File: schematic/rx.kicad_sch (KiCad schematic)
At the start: 32 parts, among them Q12 2N3904, U11 ADE-1L

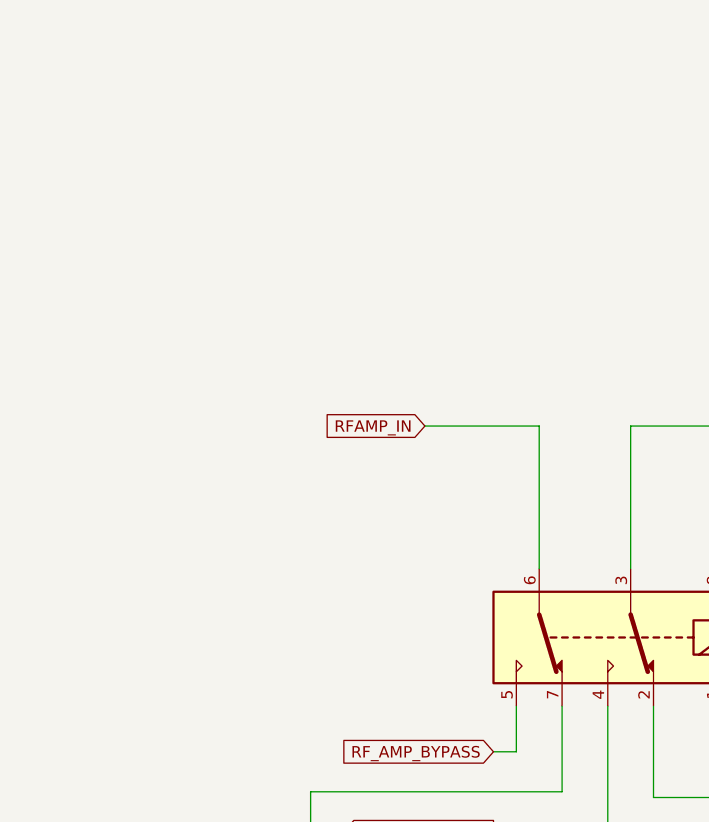
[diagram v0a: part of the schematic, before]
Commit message: Add /TX Common/ schematic sheet
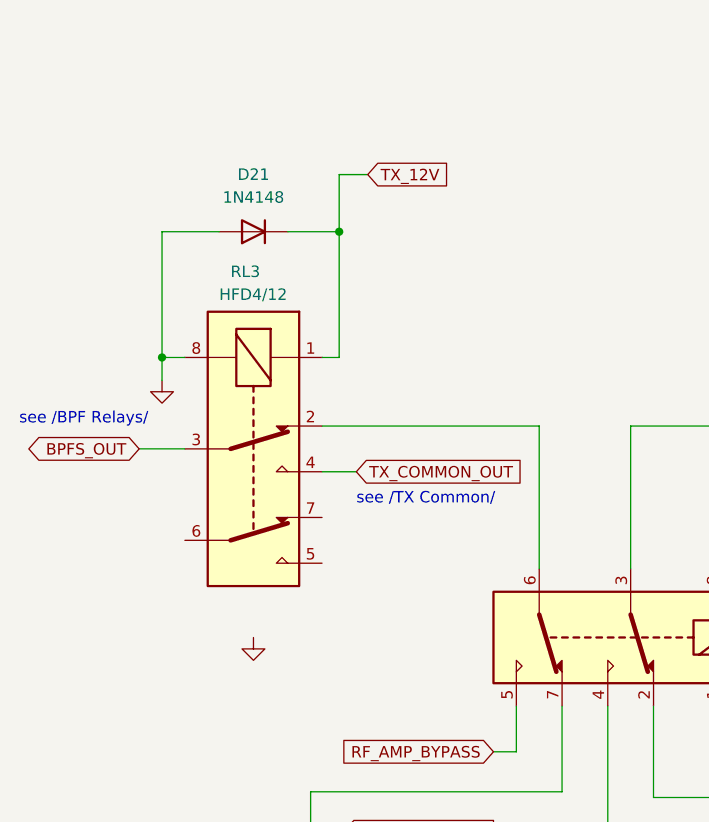
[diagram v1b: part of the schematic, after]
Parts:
- added D21: 1N4148, Diode_THT:D_DO-35_SOD27_P7.62mm_Horizontal, symbol Diode:1N4148
- added RL3: HFD4/12, Relay_THT:Relay_DPDT_Omron_G2RL, symbol Relay:G2RL-2-ASI-DC5
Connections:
- net GND: now also D21.2 (A), RL3.8
- net RFAMP_IN: no longer names the net of RL3.6
- net RFAMP_IN: now also RL3.2
- new net BPFS_OUT: RL3.3
- new net TX_12V: D21.1 (K), RL3.1
- new net TX_COMMON_OUT: RL3.4
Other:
- note added: "see /BPF Relays/"
- note added: "see /TX Common/"
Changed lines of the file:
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@@
   (junction (at 175.895 71.755) (diameter 0) (color 0 0 0 0)
   )
+  (junction (at 52.705 43.18) (diameter 0) (color 0 0 0 0)
+  )
+  (junction (at 33.02 57.15) (diameter 0) (color 0 0 0 0)
+  )
   (junction (at 196.215 45.085) (diameter 0) (color 0 0 0 0)
   )
@@
     (stroke (width 0) (type default))
   )
+  (wire (pts (xy 33.02 57.15) (xy 35.56 57.15))
+    (stroke (width 0) (type default))
+  )
   (wire (pts (xy 85.725 128.27) (xy 85.725 142.24))
     (stroke (width 0) (type default))
   )
+  (wire (pts (xy 33.02 43.18) (xy 39.37 43.18))
+    (stroke (width 0) (type default))
+  )
   (wire (pts (xy 220.98 75.565) (xy 220.98 78.105))
     (stroke (width 0) (type default))
@@
     (stroke (width 0) (type default))
   )
-  (wire (pts (xy 62.23 64.77) (xy 74.93 64.77))
+  (wire (pts (xy 50.8 64.77) (xy 74.93 64.77))
     (stroke (width 0) (type default))
   )
@@
     (stroke (width 0) (type default))
   )
+  (wire (pts (xy 33.02 57.15) (xy 33.02 43.18))
+    (stroke (width 0) (type default))
+  )
   (wire (pts (xy 174.625 52.07) (xy 175.895 52.07))
     (stroke (width 0) (type default))
@@
     (stroke (width 0) (type default))
   )
+  (wire (pts (xy 46.99 43.18) (xy 52.705 43.18))
+    (stroke (width 0) (type default))
+  )
+  (wire (pts (xy 52.705 36.83) (xy 52.705 43.18))
+    (stroke (width 0) (type default))
+  )
   (wire (pts (xy 189.23 31.115) (xy 200.025 31.115))
     (stroke (width 0) (type default))
@@
     (stroke (width 0) (type default))
   )
+  (wire (pts (xy 33.02 59.69) (xy 33.02 57.15))
+    (stroke (width 0) (type default))
+  )
   (wire (pts (xy 112.395 161.925) (xy 116.205 161.925))
     (stroke (width 0) (type default))
@@
     (stroke (width 0) (type default))
   )
+  (wire (pts (xy 52.705 43.18) (xy 52.705 57.15))
+    (stroke (width 0) (type default))
+  )
   (wire (pts (xy 95.25 97.79) (xy 111.76 97.79))
     (stroke (width 0) (type default))
@@
     (stroke (width 0) (type default))
   )
+  (wire (pts (xy 50.8 69.85) (xy 54.61 69.85))
+    (stroke (width 0) (type default))
+  )
   (wire (pts (xy 179.07 31.115) (xy 184.15 31.115))
     (stroke (width 0) (type default))
@@
     (stroke (width 0) (type default))
   )
+  (wire (pts (xy 55.88 36.83) (xy 52.705 36.83))
+    (stroke (width 0) (type default))
+  )
   (wire (pts (xy 220.98 64.77) (xy 226.695 64.77))
     (stroke (width 0) (type default))
   )
+  (wire (pts (xy 52.705 57.15) (xy 50.8 57.15))
+    (stroke (width 0) (type default))
+  )
   (wire (pts (xy 82.55 179.07) (xy 82.55 181.61))
     (stroke (width 0) (type default))
@@
   )
   (wire (pts (xy 82.55 149.225) (xy 82.55 156.845))
+    (stroke (width 0) (type default))
+  )
+  (wire (pts (xy 30.48 67.31) (xy 35.56 67.31))
     (stroke (width 0) (type default))
   )
@@
     (effects (font (size 1.27 1.27)) (justify left bottom))
   )
+  (text "see /TX Common/" (at 54.61 73.66 0)
+    (effects (font (size 1.27 1.27)) (justify left bottom))
+  )
+  (text "see /BPF Relays/" (at 17.145 64.77 0)
+    (effects (font (size 1.27 1.27)) (justify left bottom))
+  )
   (text "10T bifilar\n@ T37-43" (at 88.9 149.225 0)
     (effects (font (size 1.27 1.27)) (justify left bottom))
@@
   (text "Buffer: amp + 6 dB attenuator" (at 168.91 104.14 0)
     (effects (font (size 1.27 1.27)) (justify left bottom))
+  )
+  (global_label "TX_12V" (shape input) (at 55.88 36.83 0) (fields_autoplaced)
+    (effects (font (size 1.27 1.27)) (justify left))
+    (property "Intersheetrefs" "${INTERSHEET_REFS}" (at 65.4381 36.83 0)
+      (effects (font (size 1.27 1.27)) (justify left) hide)
+    )
   )
   (global_label "XFLT_RX_IN" (shape output) (at 226.695 64.77 0) (fields_autoplaced)
@@
     )
   )
-  (global_label "RFAMP_IN" (shape input) (at 62.23 64.77 180) (fields_autoplaced)
-    (effects (font (size 1.27 1.27)) (justify right))
-    (property "Intersheetrefs" "${INTERSHEET_REFS}" (at 50.2527 64.77 0)
-      (effects (font (size 1.27 1.27)) (justify right) hide)
-    )
-  )
   (global_label "RF_AMP_BYPASS" (shape input) (at 69.85 100.965 180) (fields_autoplaced)
     (effects (font (size 1.27 1.27)) (justify right))
@@
     )
   )
+  (global_label "BPFS_OUT" (shape bidirectional) (at 30.48 67.31 180) (fields_autoplaced)
+    (effects (font (size 1.27 1.27)) (justify right))
+    (property "Intersheetrefs" "${INTERSHEET_REFS}" (at 17.0286 67.31 0)
+      (effects (font (size 1.27 1.27)) (justify right) hide)
+    )
+  )
   (global_label "RF_AMP_BYPASS" (shape output) (at 69.85 109.855 180) (fields_autoplaced)
     (effects (font (size 1.27 1.27)) (justify right))
@@
     )
   )
+  (global_label "TX_COMMON_OUT" (shape input) (at 54.61 69.85 0) (fields_autoplaced)
+    (effects (font (size 1.27 1.27)) (justify left))
+    (property "Intersheetrefs" "${INTERSHEET_REFS}" (at 73.421 69.85 0)
+      (effects (font (size 1.27 1.27)) (justify left) hide)
+    )
+  )
   (global_label "RX_12V" (shape input) (at 196.85 17.145 180) (fields_autoplaced)
     (effects (font (size 1.27 1.27)) (justify right))
@@
     )
   )
+  (symbol (lib_id "Diode:1N4148") (at 43.18 43.18 180) (unit 1)
+    (in_bom yes) (on_board yes) (dnp no) (fields_autoplaced)
+    (property "Reference" "D21" (at 43.18 36.83 0)
+      (effects (font (size 1.27 1.27)))
+    )
+    (property "Value" "1N4148" (at 43.18 39.37 0)
+      (effects (font (size 1.27 1.27)))
+    )
+    (property "Footprint" "Diode_THT:D_DO-35_SOD27_P7.62mm_Horizontal" (at 43.18 43.18 0)
+      (effects (font (size 1.27 1.27)) hide)
+    )
+    (property "Datasheet" "https://assets.nexperia.com/documents/data-sheet/1N4148_1N4448.pdf" (at 43.18 43.18 0)
+      (effects (font (size 1.27 1.27)) hide)
+    )
+    (property "Sim.Device" "D" (at 43.18 43.18 0)
+      (effects (font (size 1.27 1.27)) hide)
+    )
+    (property "Sim.Pins" "1=K 2=A" (at 43.18 43.18 0)
+      (effects (font (size 1.27 1.27)) hide)
+    )
+    (pin "1")
+    (pin "2")
+    (instances
+      (project "hbr-mk2"
+        (path "/700c9878-4ed7-49d5-a273-77cf9d92989d/510b993f-d652-41da-8b0c-b7668be8d7c3"
+          (reference "D21") (unit 1)
+        )
+      )
+    )
+  )
   (symbol (lib_id "power:GND") (at 200.025 43.815 0) (unit 1)
     (in_bom yes) (on_board yes) (dnp no) (fields_autoplaced)
@@
     )
   )
+  (symbol (lib_id "power:GND") (at 33.02 59.69 0) (unit 1)
+    (in_bom yes) (on_board yes) (dnp no) (fields_autoplaced)
+    (property "Reference" "#PWR0130" (at 33.02 66.04 0)
+      (effects (font (size 1.27 1.27)) hide)
+    )
+    (property "Value" "GND" (at 33.02 64.77 0)
+      (effects (font (size 1.27 1.27)) hide)
+    )
+    (property "Footprint" "" (at 33.02 59.69 0)
+      (effects (font (size 1.27 1.27)) hide)
+    )
+    (property "Datasheet" "" (at 33.02 59.69 0)
+      (effects (font (size 1.27 1.27)) hide)
+    )
+    (pin "1")
+    (instances
+      (project "hbr-mk2"
+        (path "/700c9878-4ed7-49d5-a273-77cf9d92989d/0b45878c-17b8-4be8-9884-0f2bddd34788"
+          (reference "#PWR0130") (unit 1)
+        )
+        (path "/700c9878-4ed7-49d5-a273-77cf9d92989d/510b993f-d652-41da-8b0c-b7668be8d7c3"
+          (reference "#PWR0253") (unit 1)
+        )
+      )
+    )
+  )
   (symbol (lib_id "Device:R") (at 215.265 64.77 90) (unit 1)
     (in_bom yes) (on_board yes) (dnp no) (fields_autoplaced)
@@
     )
   )
+  (symbol (lib_id "Relay:G2RL-2-ASI-DC5") (at 43.18 67.31 270) (unit 1)
+    (in_bom yes) (on_board yes) (dnp no)
+    (property "Reference" "RL3" (at 40.64 47.625 90)
+      (effects (font (size 1.27 1.27)) (justify left))
+    )
+    (property "Value" "HFD4/12" (at 39.37 50.165 90)
+      (effects (font (size 1.27 1.27)) (justify left))
+    )
+    (property "Footprint" "Relay_THT:Relay_DPDT_Omron_G2RL" (at 41.91 83.82 0)
+      (effects (font (size 1.27 1.27)) (justify left) hide)
+    )
+    (property "Datasheet" "https://omronfs.omron.com/en_US/ecb/products/pdf/en-g2rl.pdf" (at 43.18 67.31 0)
+      (effects (font (size 1.27 1.27)) hide)
+    )
+    (pin "1")
+    (pin "2")
+    (pin "3")
+    (pin "4")
+    (pin "5")
+    (pin "6")
+    (pin "7")
+    (pin "8")
+    (instances
+      (project "hbr-mk2"
+        (path "/700c9878-4ed7-49d5-a273-77cf9d92989d/f830f485-dae1-49b8-8b15-2f9b2d30db58"
+          (reference "RL3") (unit 1)
+        )
+        (path "/700c9878-4ed7-49d5-a273-77cf9d92989d/4a33e42c-b3be-4c3a-afde-bb63d1cdac9b"
+          (reference "RL7") (unit 1)
+        )
+        (path "/700c9878-4ed7-49d5-a273-77cf9d92989d/f4ed3a4d-9175-4bdf-997e-86328a748647"
+          (reference "RL8") (unit 1)
+        )
+        (path "/700c9878-4ed7-49d5-a273-77cf9d92989d/510b993f-d652-41da-8b0c-b7668be8d7c3"
+          (reference "RL25") (unit 1)
+        )
+      )
+    )
+  )
   (symbol (lib_id "Device:C") (at 201.93 64.77 90) (unit 1)
     (in_bom yes) (on_board yes) (dnp no) (fields_autoplaced)
@@
         )
       )
+    )
+  )
+  (symbol (lib_id "power:GND") (at 43.18 88.265 0) (unit 1)
+    (in_bom yes) (on_board yes) (dnp no) (fields_autoplaced)
+    (property "Reference" "#PWR0130" (at 43.18 94.615 0)
+      (effects (font (size 1.27 1.27)) hide)
+    )
+    (property "Value" "GND" (at 43.18 93.345 0)
+      (effects (font (size 1.27 1.27)) hide)
+    )
+    (property "Footprint" "" (at 43.18 88.265 0)
+      (effects (font (size 1.27 1.27)) hide)
+    )
+    (property "Datasheet" "" (at 43.18 88.265 0)
+      (effects (font (size 1.27 1.27)) hide)
+    )
+    (pin "1")
+    (instances
+      (project "hbr-mk2"
+        (path "/700c9878-4ed7-49d5-a273-77cf9d92989d/0b45878c-17b8-4be8-9884-0f2bddd34788"
+          (reference "#PWR0130") (unit 1)
+        )
+        (path "/700c9878-4ed7-49d5-a273-77cf9d92989d/510b993f-d652-41da-8b0c-b7668be8d7c3"
+          (reference "#PWR0252") (unit 1)
+        )
+      )

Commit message: Schematic: minor changes
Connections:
- net GND: now also RL3.5, RL3.6, RL3.7
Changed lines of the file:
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@@
   (junction (at 82.55 149.225) (diameter 0) (color 0 0 0 0)
   )
+  (junction (at 55.245 80.01) (diameter 0) (color 0 0 0 0)
+  )
   (junction (at 209.55 64.77) (diameter 0) (color 0 0 0 0)
   )
@@
   (junction (at 33.02 57.15) (diameter 0) (color 0 0 0 0)
   )
+  (junction (at 43.18 85.09) (diameter 0) (color 0 0 0 0)
+  )
   (junction (at 196.215 45.085) (diameter 0) (color 0 0 0 0)
   )
@@
     (stroke (width 0) (type default))
   )
+  (wire (pts (xy 32.385 77.47) (xy 32.385 85.09))
+    (stroke (width 0) (type default))
+  )
   (wire (pts (xy 209.55 75.565) (xy 209.55 77.47))
     (stroke (width 0) (type default))
@@
     (stroke (width 0) (type default))
   )
+  (wire (pts (xy 50.8 80.01) (xy 55.245 80.01))
+    (stroke (width 0) (type default))
+  )
   (wire (pts (xy 220.98 75.565) (xy 220.98 78.105))
     (stroke (width 0) (type default))
   )
+  (wire (pts (xy 55.245 74.93) (xy 50.8 74.93))
+    (stroke (width 0) (type default))
+  )
   (wire (pts (xy 71.12 161.925) (xy 72.39 161.925))
     (stroke (width 0) (type default))
@@
     (stroke (width 0) (type default))
   )
+  (wire (pts (xy 43.18 85.09) (xy 43.18 88.265))
+    (stroke (width 0) (type default))
+  )
   (wire (pts (xy 196.215 45.085) (xy 196.215 64.77))
     (stroke (width 0) (type default))
@@
     (stroke (width 0) (type default))
   )
+  (wire (pts (xy 55.245 80.01) (xy 55.245 74.93))
+    (stroke (width 0) (type default))
+  )
   (wire (pts (xy 33.02 59.69) (xy 33.02 57.15))
     (stroke (width 0) (type default))
@@
     (stroke (width 0) (type default))
   )
+  (wire (pts (xy 43.18 85.09) (xy 55.245 85.09))
+    (stroke (width 0) (type default))
+  )
+  (wire (pts (xy 55.245 85.09) (xy 55.245 80.01))
+    (stroke (width 0) (type default))
+  )
   (wire (pts (xy 52.705 43.18) (xy 52.705 57.15))
     (stroke (width 0) (type default))
@@
     (stroke (width 0) (type default))
   )
+  (wire (pts (xy 32.385 85.09) (xy 43.18 85.09))
+    (stroke (width 0) (type default))
+  )
   (wire (pts (xy 72.39 100.965) (xy 72.39 95.885))
     (stroke (width 0) (type default))
@@
     (stroke (width 0) (type default))
   )
+  (wire (pts (xy 35.56 77.47) (xy 32.385 77.47))
+    (stroke (width 0) (type default))
+  )

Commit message: Minor changes
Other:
- moved on the sheet: C78, C79, C80, C81, C82, D14, D21, L12, Q12, R58, R59, R60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

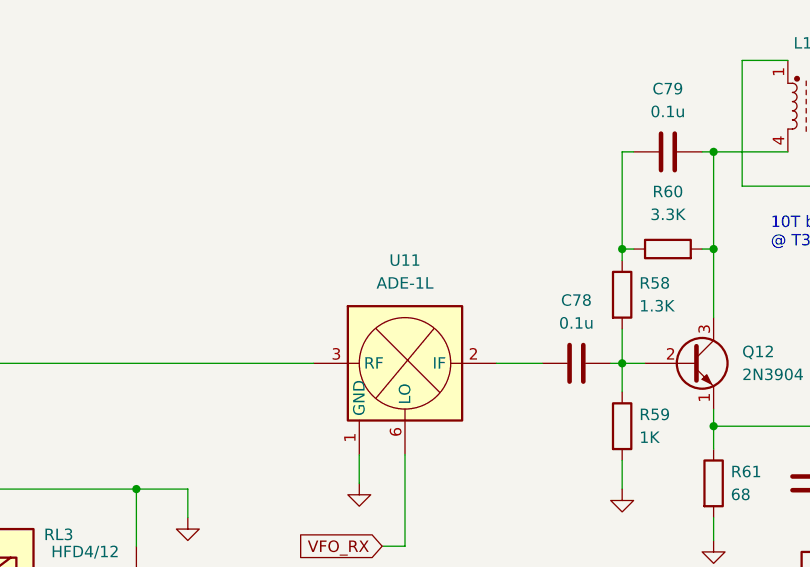
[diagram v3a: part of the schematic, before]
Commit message: Schematic: minor changes
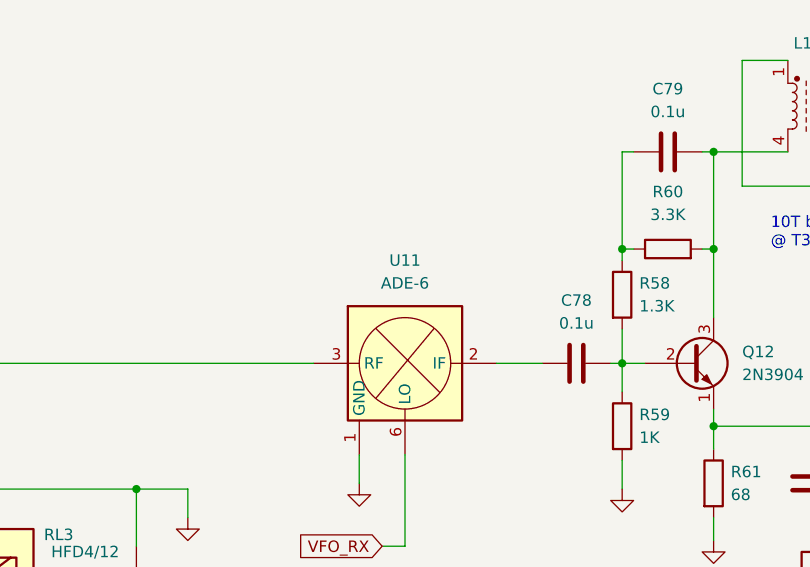
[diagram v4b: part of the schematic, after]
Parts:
- U11: value ADE-1L -> ADE-6
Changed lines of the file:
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@@
       (effects (font (size 1.27 1.27)))
     )
-    (property "Value" "ADE-1L" (at 169.545 56.515 0)
+    (property "Value" "ADE-6" (at 169.545 56.515 0)
       (effects (font (size 1.27 1.27)))
     )

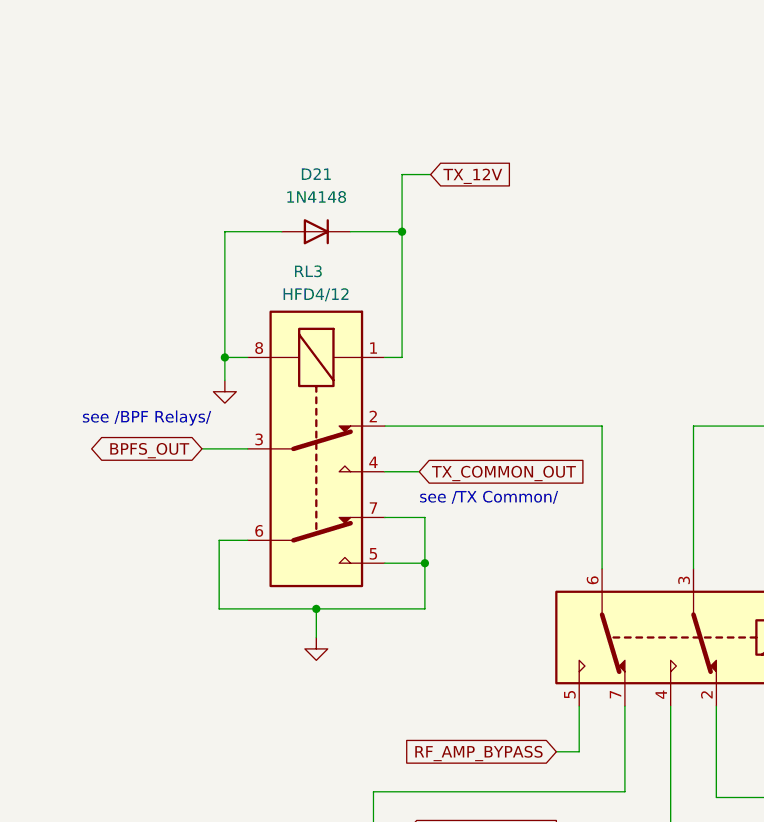
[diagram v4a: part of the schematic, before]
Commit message: Connect relay contact groups in parallel where appropriate
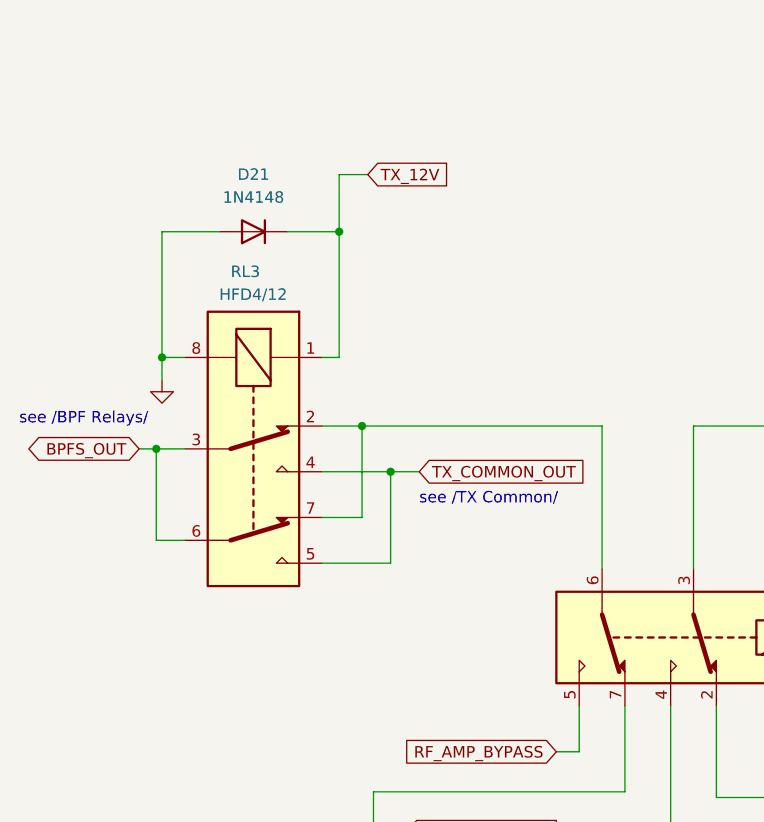
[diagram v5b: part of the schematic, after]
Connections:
- net BPFS_OUT: now also RL3.6
- net GND: no longer RL3.5, RL3.6, RL3.7
- net TX_COMMON_OUT: now also RL3.5
- net at RL3.2, RL3.6: now also RL3.7
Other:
- moved on the sheet: D21, RL3

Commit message: Add PA schematic + some minor changes
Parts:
- L12: value L_Ferrite_Coupled_1423 -> FT37-43
- L12: value L_Ferrite_Coupled_1423 -> T37-43
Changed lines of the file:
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@@
       (effects (font (size 1.27 1.27)) (justify left))
     )
-    (property "Value" "L_Ferrite_Coupled_1423" (at 211.455 37.846 90)
+    (property "Value" "FT37-43" (at 211.455 37.846 90)
       (effects (font (size 1.27 1.27)) (justify left) hide)
     )
@@
       (effects (font (size 1.27 1.27)) (justify left))
     )
-    (property "Value" "L_Ferrite_Coupled_1423" (at 118.745 135.001 90)
+    (property "Value" "T37-43" (at 118.745 135.001 90)
       (effects (font (size 1.27 1.27)) (justify left) hide)
     )

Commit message: Schematic: minor fixes
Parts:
- L12: value T37-43 -> FT37-43
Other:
- note added: "10T bifilar @ FT37-43"
- note removed: "10T bifilar @ T37-43"
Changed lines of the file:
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@@
     (effects (font (size 1.27 1.27)) (justify left bottom))
   )
-  (text "10T bifilar\n@ T37-43" (at 210.185 52.705 0)
+  (text "10T bifilar\n@ FT37-43" (at 210.185 52.705 0)
     (effects (font (size 1.27 1.27)) (justify left bottom))
   )
@@
     (effects (font (size 1.27 1.27)) (justify left bottom))
   )
-  (text "10T bifilar\n@ T37-43" (at 116.84 149.86 0)
+  (text "10T bifilar\n@ FT37-43" (at 116.84 149.86 0)
     (effects (font (size 1.27 1.27)) (justify left bottom))
   )
@@
       (effects (font (size 1.27 1.27)) (justify left))
     )
-    (property "Value" "T37-43" (at 118.745 135.001 90)
-      (effects (font (size 1.27 1.27)) (justify left) hide)
-    )
+    (property "Value" "FT37-43" (at 118.745 135.001 90)
+      (effects (font (size 1.27 1.27)) (justify left) hide)
+    )
